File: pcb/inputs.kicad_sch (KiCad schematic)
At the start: 91 parts, among them Q7 NPN, Q8 BC858, SW1 SW_Push

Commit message: Haven't backed up in a bit
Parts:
- added D43, D44, D45, D46, D47, D48: D_Small, Diode_SMD:D_SOD-123, symbol Device:D_Small
- added SW1 (x6): SW_Push, local-library:SW_PG1350, symbol Switch:SW_Push
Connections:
- net col10: now also SW1.2
- net col6: no longer SW1.2
- net col7: no longer SW1.2
- net col8: now also SW1.2; no longer SW1.2
- net col9: now also SW1.2
- net row0: now also D43.1 (K), D46.1 (K)
- net row1: now also D44.1 (K), D47.1 (K)
- net row2: now also D45.1 (K), D48.1 (K)
- new net: D48.2 (A), SW1.1
- new net: D46.2 (A), SW1.1
- new net: D44.2 (A), SW1.1
- new net: D45.2 (A), SW1.1
- new net: D43.2 (A), SW1.1
- new net: D47.2 (A), SW1.1
- new net col12: SW1.2, SW1.2, SW1.2
- new net col13: SW1.2, SW1.2, SW1.2
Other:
- moved on the sheet: D25, D29, D33, SW1

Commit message: Schematic done, starting PCB design
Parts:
- removed Q7: NPN, symbol Simulation_SPICE:NPN
- removed Q8: BC858, Package_TO_SOT_SMD:SOT-23, symbol Transistor_BJT:BC858
- removed R18, R19, R20: 10k, symbol Device:R
- removed R21, R22: 100, symbol Device:R
- added Q1: BC858, Package_TO_SOT_SMD:SOT-23, symbol Transistor_BJT:BC858
- added R10, R8: 10k, Resistor_SMD:R_0603_1608Metric_Pad0.98x0.95mm_HandSolder, symbol Device:R
- added R5: 1k, Resistor_SMD:R_0603_1608Metric_Pad0.98x0.95mm_HandSolder, symbol Device:R
- renumbered D9 to D10, D10 to D11, D11 to D12, D12 to D13, D13 to D14, D14 to D15, D15 to D16, D16 to D17, D17 to D18, D18 to D19, D1 to D2, D19 to D20, D20 to D21, D21 to D22, D22 to D23, D23 to D24, D24 to D25, D30 to D29, D2 to D3, D31 to D30, D32 to D31, D25 to D32, D34 to D33, D35 to D34, D36 to D35, D29 to D36, D3 to D4, D33 to D40, D40 to D41, D41 to D42, D42 to D43, D43 to D44, D44 to D45, D45 to D46, D46 to D47, D47 to D48, D48 to D49, D4 to D5, D5 to D6, D6 to D7, D7 to D8, D8 to D9
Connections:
- net +3.3V is gone; now on net GND: SW1.1
- net GND: now also R10.2
- net S1_OUT: now also Q1.3 (C), R10.1
- net col0: now also Q1.2 (E)
- net BOOT0 renamed BOOT
- net BOOT: now also R5.1, R8.2
- new net: Q1.1 (B), R5.2
- new net +3V3: R8.1
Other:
- note added: "BOOT button"
- note added: "Pull boot high by default"
- note added: "This circuit pulls BOOT low during startup to enter USB boot mode, this allows us to flash the board without opening up the case, by using a key that doubles as a boot button"
- note removed: "BOOT0 button"
- note removed: "NOTE:"
- note removed: "Pulled high on button press"
- note removed: "Pulled high on button press and col0 high"
- note removed: "Replace 100R with whatever we're using for an indicator LED"
- moved on the sheet: D10, D11, D12, D13, D14, D15, D16, D17, D18, D19, D2, D20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

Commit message: Switches placement done, updated footprints to include model
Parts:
- added D26, D30: D_Small, Diode_SMD:D_SOD-123, symbol Device:D_Small
- added SW1 (x2): SW_Push, local-library:SW_PG1350, symbol Switch:SW_Push
- renumbered D26 to D27, D27 to D28, D28 to D29, D29 to D31, D30 to D32, D31 to D33, D32 to D34, D33 to D35, D34 to D36, D35 to D37, D36 to D38, D37 to D39, D38 to D40, D39 to D41, D40 to D42, D41 to D43, D42 to D44, D43 to D45, D44 to D46, D45 to D47, D46 to D48, D47 to D49, D48 to D50, D49 to D51
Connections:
- net col6: now also SW1.2
- net col7: now also SW1.2
- net row3: now also D26.1 (K), D30.1 (K)
- new net: D26.2 (A), SW1.1
- new net: D30.2 (A), SW1.1

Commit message: Routing in progress
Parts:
- removed SW1 (x2): SW_Push, local-library:SW_PG1350, symbol Switch:SW_Push
- added SW1 (x2): SW_Push, local-library:SW_PG1350, symbol Switch:SW_Push
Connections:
- net col0: now also SW1.2; no longer Q1.2 (E)
- net col13: now also SW1.2
- net col7: now also Q1.2 (E)
- net at D49.2 (A): now also SW1.1
- net SS_OUT: now reaches D27.2 (A)
- net SS_OUT: now also Q1.3 (C), R10.1
- removed net S1_OUT: D2.2 (A), Q1.3 (C), R10.1
- new net: D2.2 (A), SW1.1

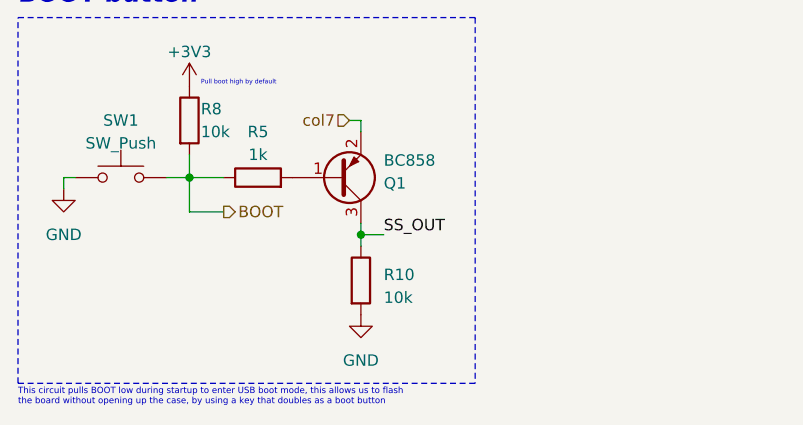
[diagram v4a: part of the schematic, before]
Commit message: Rerouted a lot of stuff
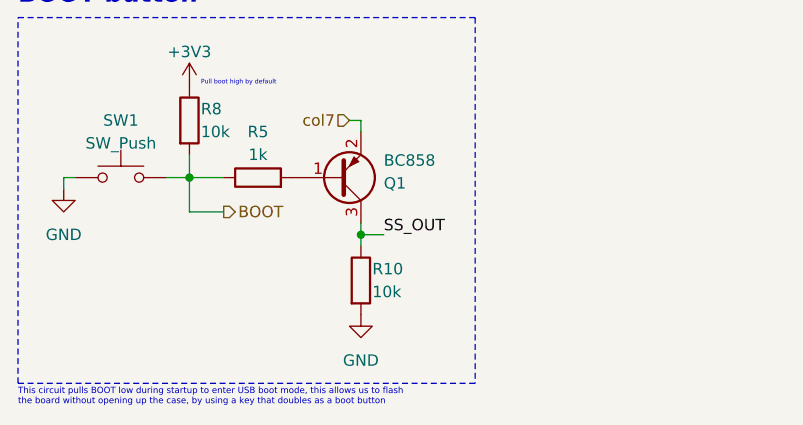
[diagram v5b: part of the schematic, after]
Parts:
- R10, R5, R8: footprint Resistor_SMD:R_0603_1608Metric_Pad0.98x0.95mm_HandSolder -> Resistor_SMD:R_0402_1005Metric
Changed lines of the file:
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@@
       (effects (font (size 1.27 1.27)))
     )
-    (property "Footprint" "Resistor_SMD:R_0603_1608Metric_Pad0.98x0.95mm_HandSolder" (at 52.07 133.858 90)
+    (property "Footprint" "Resistor_SMD:R_0402_1005Metric" (at 52.07 133.858 90)
       (effects (font (size 1.27 1.27)) hide)
     )
@@
       (effects (font (size 1.27 1.27)) (justify left))
     )
-    (property "Footprint" "Resistor_SMD:R_0603_1608Metric_Pad0.98x0.95mm_HandSolder" (at 42.672 125.73 90)
+    (property "Footprint" "Resistor_SMD:R_0402_1005Metric" (at 42.672 125.73 90)
       (effects (font (size 1.27 1.27)) hide)
     )
@@
         (path "/fc529d87-72d0-4c92-b352-ddcf4c6f7199/1c8ac5bd-b3bc-4835-a71b-e635010cd696"
           (reference "D10") (unit 1)
+        )
+      )
+    )
+  )
+  (symbol (lib_id "Device:R") (at 63.5 143.51 0) (unit 1)
+    (in_bom yes) (on_board yes) (dnp no)
+    (property "Reference" "R10" (at 64.77 142.24 0)
+      (effects (font (size 1.27 1.27)) (justify left))
+    )
+    (property "Value" "10k" (at 64.77 144.78 0)
+      (effects (font (size 1.27 1.27)) (justify left))
+    )
+    (property "Footprint" "Resistor_SMD:R_0402_1005Metric" (at 61.722 143.51 90)
+      (effects (font (size 1.27 1.27)) hide)
+    )
+    (property "Datasheet" "~" (at 63.5 143.51 0)
+      (effects (font (size 1.27 1.27)) hide)
+    )
+    (pin "1")
+    (pin "2")
+    (instances
+      (project "keyboard"
+        (path "/fc529d87-72d0-4c92-b352-ddcf4c6f7199/1c8ac5bd-b3bc-4835-a71b-e635010cd696"
+          (reference "R10") (unit 1)
         )
       )
@@
         )
       )
-    )
-  )
-  (symbol (lib_id "Device:R") (at 63.5 143.51 0) (unit 1)
-    (in_bom yes) (on_board yes) (dnp no) (fields_autoplaced)
-    (property "Reference" "R10" (at 66.04 142.875 0)
-      (effects (font (size 1.27 1.27)) (justify left))
-    )
-    (property "Value" "10k" (at 66.04 145.415 0)
-      (effects (font (size 1.27 1.27)) (justify left))
-    )
-    (property "Footprint" "Resistor_SMD:R_0603_1608Metric_Pad0.98x0.95mm_HandSolder" (at 61.722 143.51 90)
-      (effects (font (size 1.27 1.27)) hide)
-    )
-    (property "Datasheet" "~" (at 63.5 143.51 0)
-      (effects (font (size 1.27 1.27)) hide)
-    )
-    (pin "1")
-    (pin "2")
-    (instances
-      (project "keyboard"
-        (path "/fc529d87-72d0-4c92-b352-ddcf4c6f7199/1c8ac5bd-b3bc-4835-a71b-e635010cd696"
-          (reference "R10") (unit 1)
-        )
-      )

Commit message: PCB design complete
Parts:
- Q1: value BC858 -> S8550; LCSC C81569 -> C105432
- R10, R8: LCSC (none) -> C25744
- R5: LCSC (none) -> C11702
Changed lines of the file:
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@@
+      (effects (font (size 1.27 1.27)) hide)
+    )
+    (property "LCSC" "C11702" (at 52.07 132.08 90)
       (effects (font (size 1.27 1.27)) hide)
     )
@@
       (effects (font (size 1.27 1.27)) hide)
     )
+    (property "LCSC" "C25744" (at 44.45 125.73 0)
+      (effects (font (size 1.27 1.27)) hide)
+    )
     (pin "1")
     (pin "2")
@@
     )
     (property "Datasheet" "~" (at 63.5 143.51 0)
+      (effects (font (size 1.27 1.27)) hide)
+    )
+    (property "LCSC" "C25744" (at 63.5 143.51 0)
       (effects (font (size 1.27 1.27)) hide)
     )
@@
       (effects (font (size 1.27 1.27)) (justify left))
     )
-    (property "Value" "BC858" (at 66.04 130.175 0)
+    (property "Value" "S8550" (at 66.04 130.175 0)
       (effects (font (size 1.27 1.27)) (justify left))
     )
@@
       (effects (font (size 1.27 1.27) italic) (justify left) hide)
     )
-    (property "Datasheet" "https://www.onsemi.com/pub/Collateral/BC860-D.pdf" (at 60.96 132.08 0)
+    (property "Datasheet" "https://wmsc.lcsc.com/wmsc/upload/file/pdf/v2/lcsc/2304140030_Foshan-NationStar-Optoelectronics-NCD0805R1_C84256.pdf" (at 60.96 132.08 0)
       (effects (font (size 1.27 1.27)) (justify left) hide)
     )
-    (property "LCSC" "C81569" (at 60.96 132.08 0)
-      (effects (font (size 1.27 1.27)) hide)
-    )
+    (property "LCSC" "C105432" (at 60.96 132.08 0)
+      (effects (font (size 1.27 1.27)) hide)
+    )
